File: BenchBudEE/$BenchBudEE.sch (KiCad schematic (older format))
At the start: 0 parts

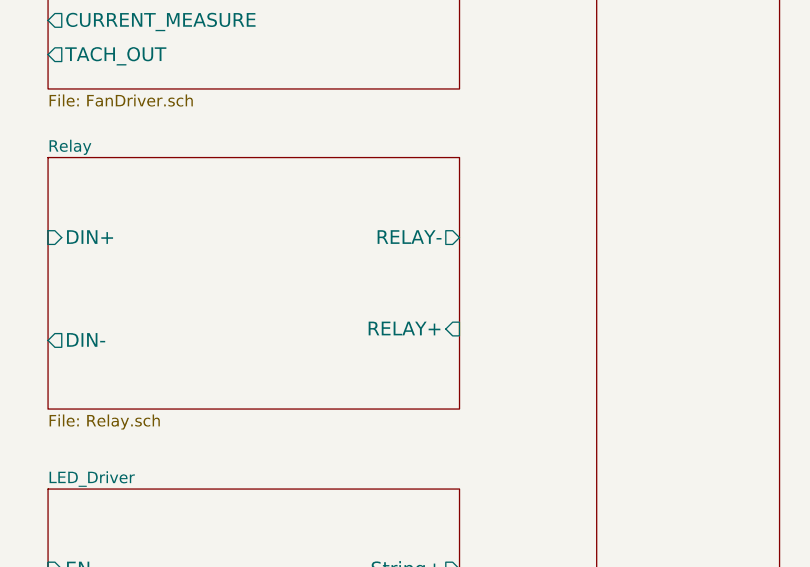
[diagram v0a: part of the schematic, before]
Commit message: Created Relay block diagram
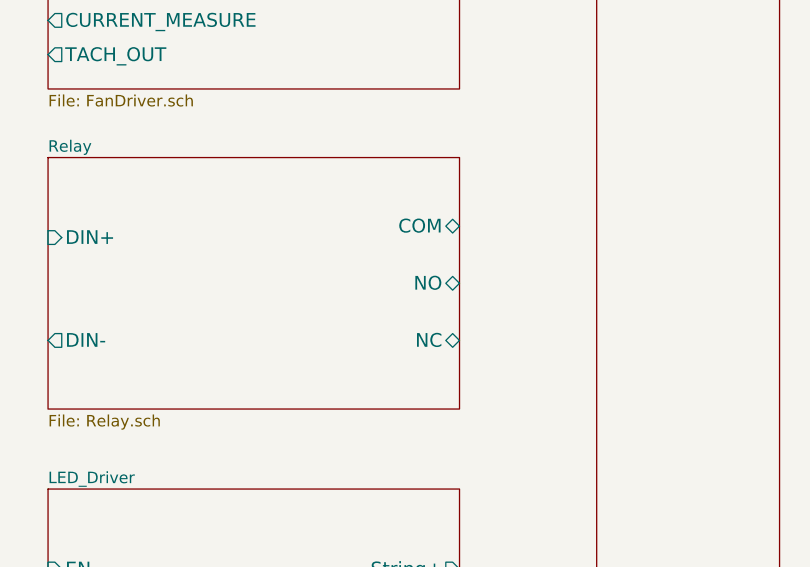
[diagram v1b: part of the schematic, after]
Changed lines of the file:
@@
 F2 "DIN+" I L 7400 4250 60
 F3 "DIN-" O L 7400 4700 60
-F4 "RELAY-" O R 9200 4250 60
-F5 "RELAY+" I R 9200 4650 60
+F4 "NO" B R 9200 4450 60
+F5 "NC" B R 9200 4700 60
+F6 "COM" B R 9200 4200 60
 $EndSheet
 $Sheet
